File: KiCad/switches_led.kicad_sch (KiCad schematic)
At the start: 70 parts, among them Q2 MMBT3904, Q3 MMBT3904, Q4 MMBT3904, Q5 MMBT3904, Q6 MMBT3904, Q7 MMBT3904, Q8 MMBT3904, Q9 MMBT3904, SW8 SW_Rotary_1x9_MP, U2 CD4017BE

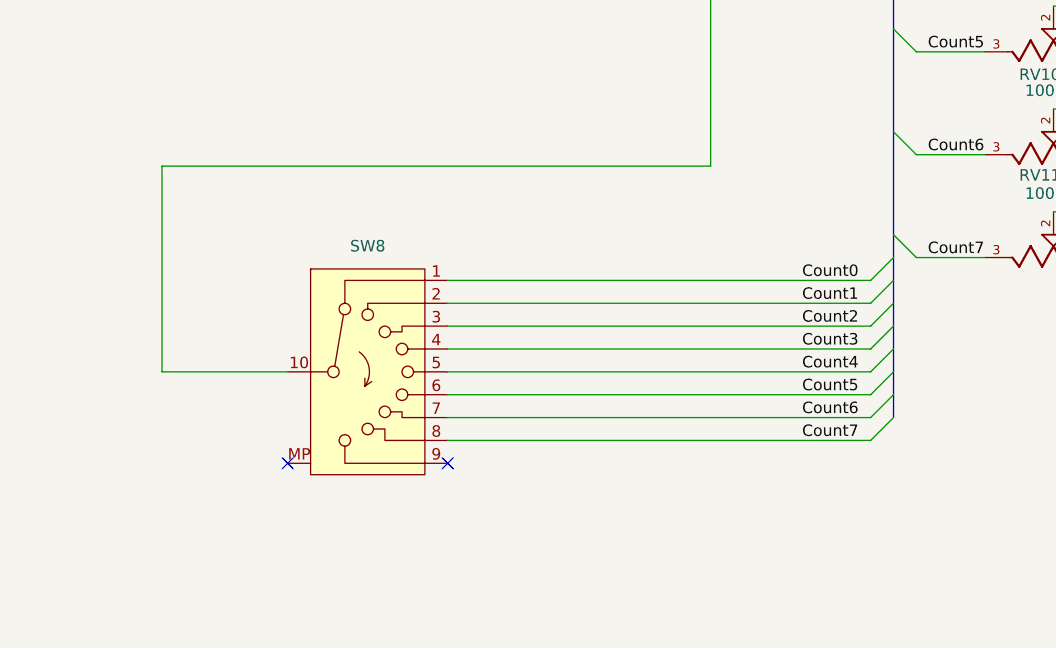
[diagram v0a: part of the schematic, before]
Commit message: adding footprint for rotary switch P1S8
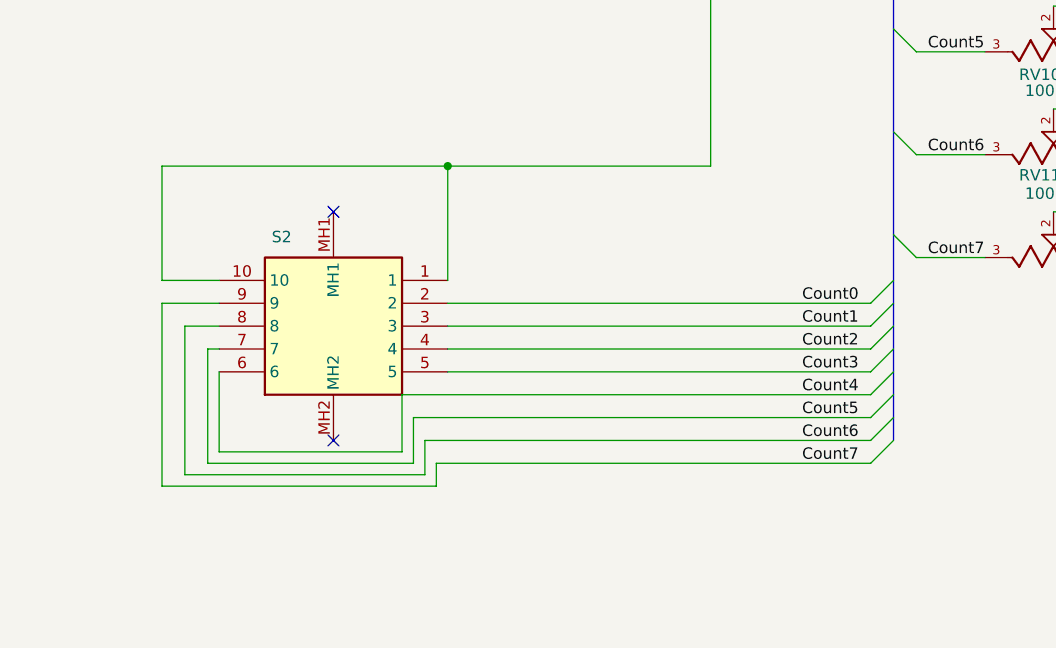
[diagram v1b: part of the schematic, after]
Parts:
- removed SW8: SW_Rotary_1x9_MP, symbol Switch:SW_Rotary_1x9_MP
- added S2: SR1712F-0108-20F0A-N9-N-027, Eurorack:1 Pole 8 Step Switch Alpha, symbol Eurorack:SR1712F-0108-20F0A-N9-N-027
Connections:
- net Count0: now also S2.2
- net Count1: now also S2.3
- net Count2: now also S2.4
- net Count3: now also S2.5
- net Count4: now also S2.6
- net Count5: now also S2.7
- net Count6: now also S2.8
- net Count7: now also S2.9
- net EXTERNAL RESET: now also S2.1, S2.10

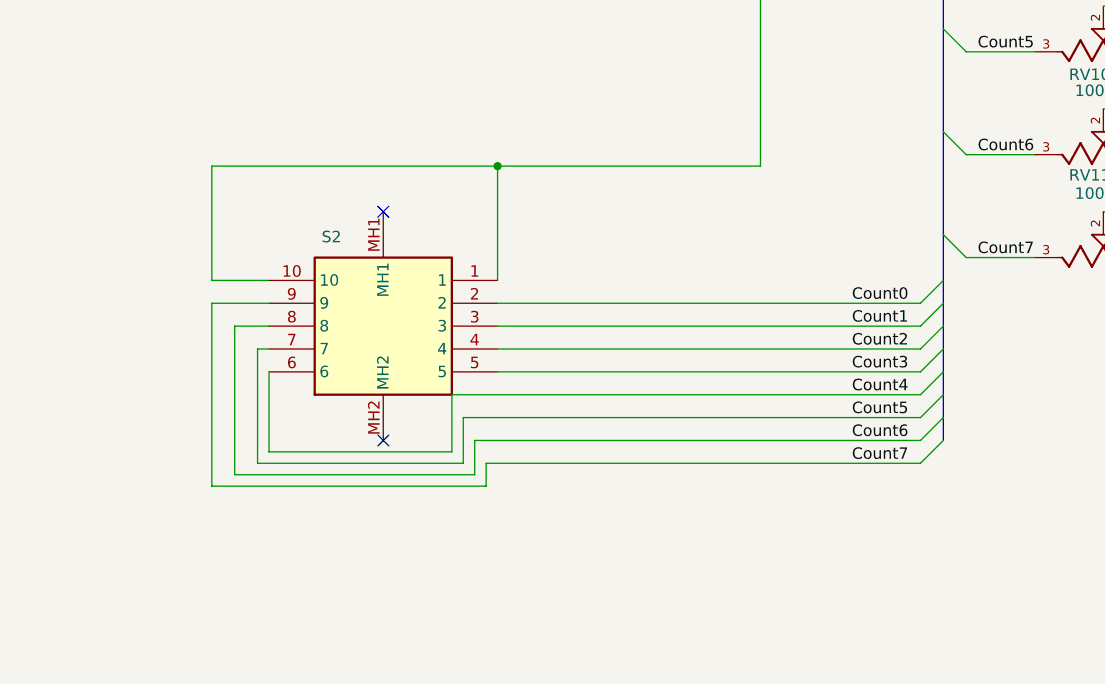
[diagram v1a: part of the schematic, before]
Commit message: adding new rotary switch
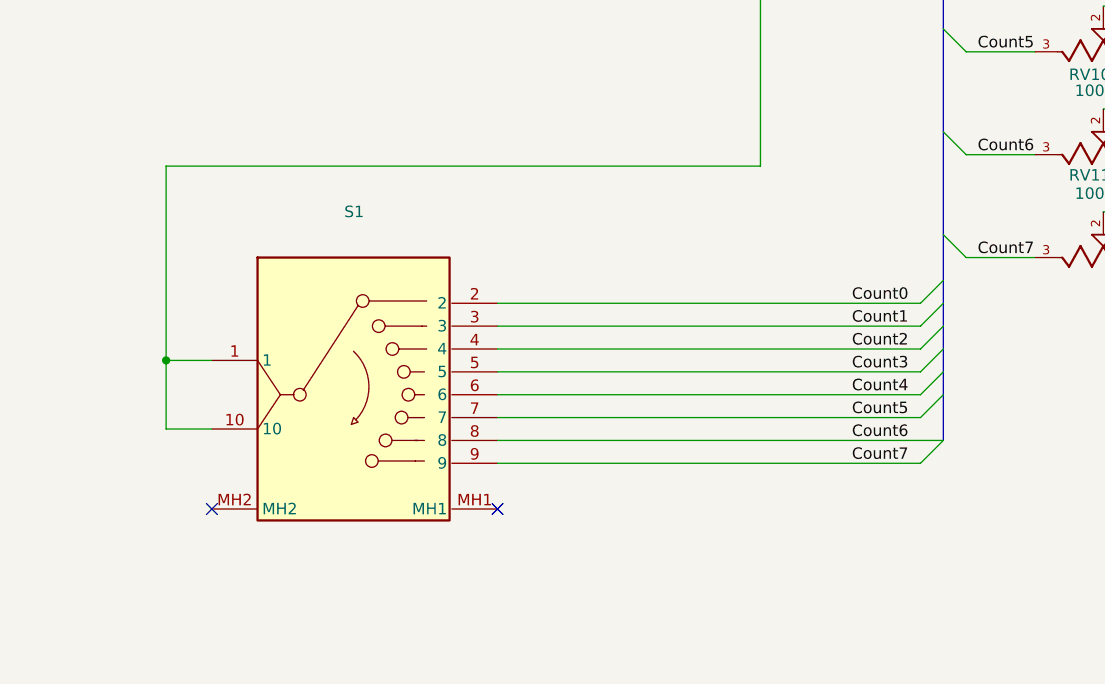
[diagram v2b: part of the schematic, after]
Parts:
- removed S2: SR1712F-0108-20F0A-N9-N-027, Eurorack:1 Pole 8 Step Switch Alpha, symbol Eurorack:SR1712F-0108-20F0A-N9-N-027
- added S1: SR1712F-0108-20F0A-N9-N-027, Eurorack:1 Pole 8 Step Switch Alpha, symbol Eurorack:SR1712F-0108-20F0A-N9-N-027
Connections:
- net Count0: now also S1.2
- net Count1: now also S1.3
- net Count2: now also S1.4
- net Count3: now also S1.5
- net Count4: now also S1.6
- net Count5: now also S1.7
- net Count6: now also S1.8
- net Count7: now also S1.9
- net EXTERNAL RESET: now also S1.1, S1.10

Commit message: placing layout frontview
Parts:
- RV10, RV11, RV4, RV5, RV6, RV7, RV8, RV9: footprint Eurorack:RD901F -> Eurorack:RD901F_1
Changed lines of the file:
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@@
 	(title_block
 		(title "8 Step Sequencer")
-		(date "2026-03-13")
+		(date "2026-03-21")
 		(rev "v1.0")
 		(company "Dirty Dream - Nathanael Noir")
@@
 			)
 		)
-		(property "Footprint" "Eurorack:RD901F"
+		(property "Footprint" "Eurorack:RD901F_1"
 			(at 247.65 52.07 0)
 			(effects
@@
 			)
 		)
-		(property "Footprint" "Eurorack:RD901F"
+		(property "Footprint" "Eurorack:RD901F_1"
 			(at 247.65 64.77 0)
 			(effects
@@
 			)
 		)
-		(property "Footprint" "Eurorack:RD901F"
+		(property "Footprint" "Eurorack:RD901F_1"
 			(at 247.65 111.76 0)
 			(effects
@@
 			)
 		)
-		(property "Footprint" "Eurorack:RD901F"
+		(property "Footprint" "Eurorack:RD901F_1"
 			(at 247.65 76.2 0)
 			(effects
@@
 			)
 		)
-		(property "Footprint" "Eurorack:RD901F"
+		(property "Footprint" "Eurorack:RD901F_1"
 			(at 247.65 100.33 0)
 			(effects
@@
 			)
 		)
-		(property "Footprint" "Eurorack:RD901F"
+		(property "Footprint" "Eurorack:RD901F_1"
 			(at 247.65 123.19 0)
 			(effects
@@
 			)
 		)
-		(property "Footprint" "Eurorack:RD901F"
+		(property "Footprint" "Eurorack:RD901F_1"
 			(at 247.65 88.9 0)
 			(effects
@@
 			)
 		)
-		(property "Footprint" "Eurorack:RD901F"
+		(property "Footprint" "Eurorack:RD901F_1"
 			(at 247.65 39.37 0)
 			(effects

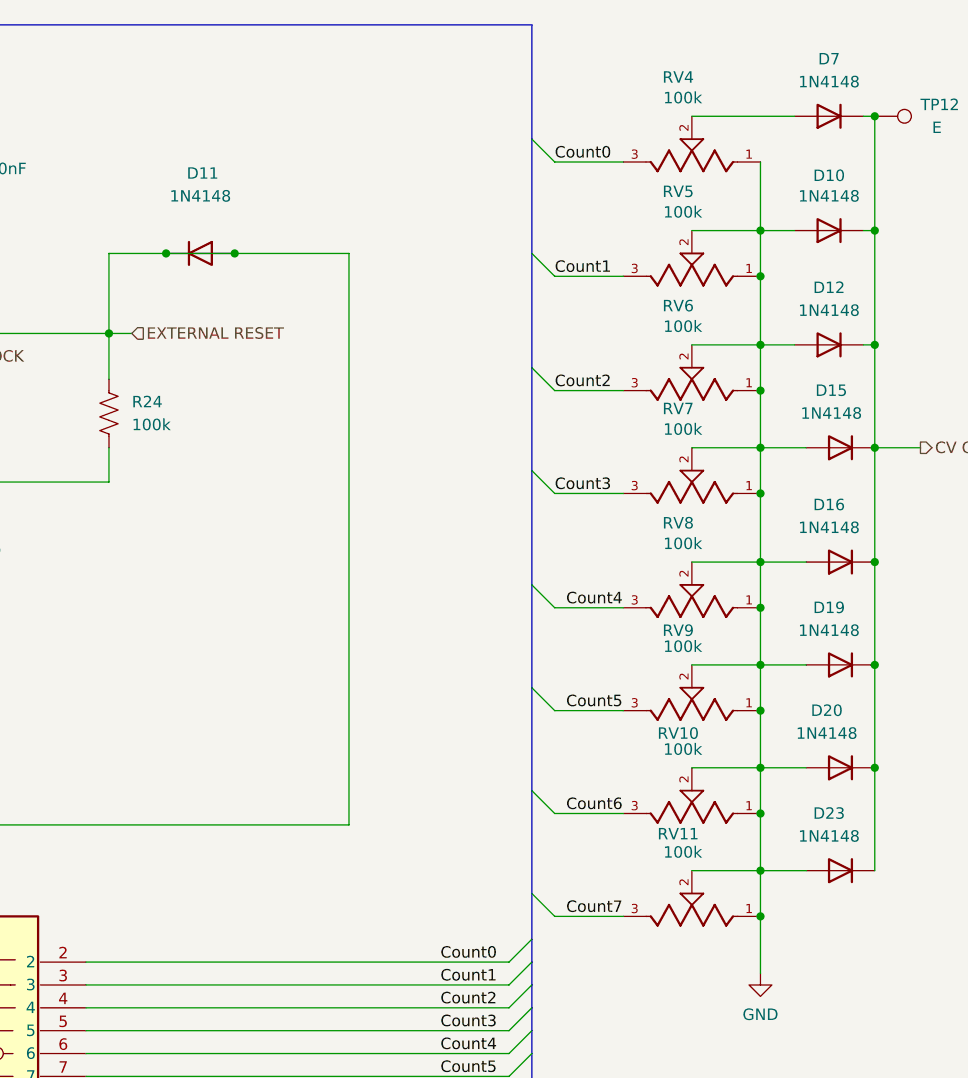
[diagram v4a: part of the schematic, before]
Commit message: fixing some errors in schematics; first component placement
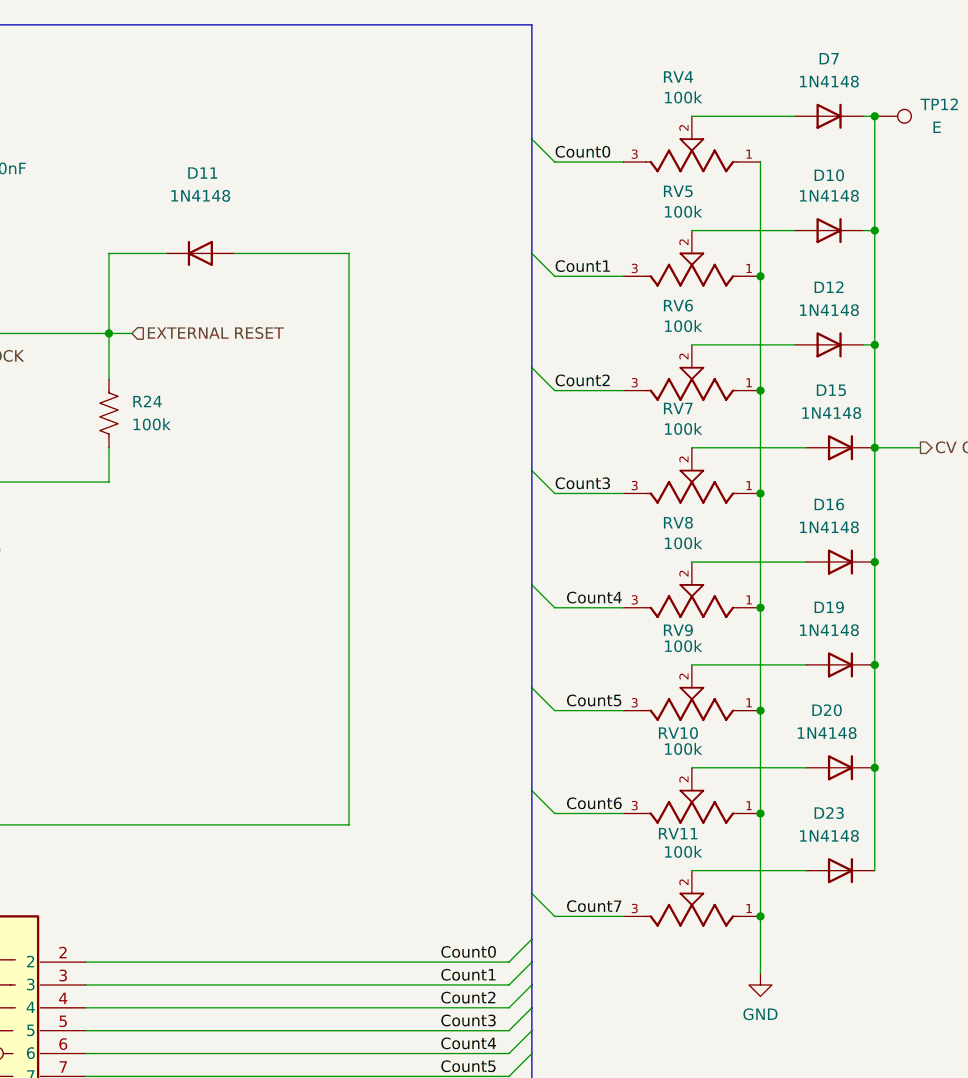
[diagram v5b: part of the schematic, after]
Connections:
- net EXTERNAL RESET: no longer D11.2 (A), S1.1, S1.10
- net GND: no longer D10.2 (A), D12.2 (A), D15.2 (A), D16.2 (A), D19.2 (A), D20.2 (A), D23.2 (A), RV10.2, RV11.2, RV5.2, RV6.2, RV7.2, RV8.2, RV9.2
- new net: D11.2 (A), S1.1, S1.10
- new net: D23.2 (A), RV11.2
- new net: D10.2 (A), RV5.2
- new net: D16.2 (A), RV8.2
- new net: D12.2 (A), RV6.2
- new net: D20.2 (A), RV10.2
- new net: D15.2 (A), RV7.2
- new net: D19.2 (A), RV9.2
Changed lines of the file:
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@@
-	)
-	(junction
-		(at 189.23 49.53)
-		(diameter 0)
-		(color 0 0 0 0)
 	)
 	(junction
@@
 	)
 	(junction
-		(at 255.27 83.82)
-		(diameter 0)
-		(color 0 0 0 0)
-	)
-	(junction
 		(at 19.05 90.17)
 		(diameter 0)
@@
 	)
 	(junction
-		(at 255.27 59.69)
-		(diameter 0)
-		(color 0 0 0 0)
-	)
-	(junction
 		(at 59.69 29.21)
 		(diameter 0)
@@
 	)
 	(junction
-		(at 255.27 46.99)
-		(diameter 0)
-		(color 0 0 0 0)
-	)
-	(junction
 		(at 83.82 90.17)
 		(diameter 0)
@@
 	)
 	(junction
-		(at 255.27 95.25)
-		(diameter 0)
-		(color 0 0 0 0)
-	)
-	(junction
 		(at 267.97 34.29)
 		(diameter 0)
@@
 	)
 	(junction
-		(at 196.85 49.53)
-		(diameter 0)
-		(color 0 0 0 0)
-	)
-	(junction
 		(at 19.05 160.02)
 		(diameter 0)
@@
 	)
 	(junction
-		(at 255.27 106.68)
-		(diameter 0)
-		(color 0 0 0 0)
-	)
-	(junction
-		(at 255.27 118.11)
-		(diameter 0)
-		(color 0 0 0 0)
-	)
-	(junction
 		(at 255.27 76.2)
-		(diameter 0)
-		(color 0 0 0 0)
-	)
-	(junction
-		(at 255.27 71.12)
 		(diameter 0)
 		(color 0 0 0 0)
@@
 		)
 	)
-	(wire
-		(pts
-			(xy 196.85 49.53) (xy 189.23 49.53)
-		)
-		(stroke
-			(width 0)
-			(type default)
-		)
-	)
-	(wire
-		(pts
-			(xy 255.27 52.07) (xy 255.27 59.69)
-		)
-		(stroke
-			(width 0)
-			(type default)
-		)
-	)
 	(bus
 		(pts
@@
 	(wire
 		(pts
-			(xy 255.27 95.25) (xy 260.35 95.25)
+			(xy 247.65 95.25) (xy 260.35 95.25)
 		)
 		(stroke
@@
 	(wire
 		(pts
-			(xy 255.27 106.68) (xy 260.35 106.68)
-		)
-		(stroke
-			(width 0)
-			(type default)
-		)
-	)
-	(wire
-		(pts
-			(xy 255.27 88.9) (xy 255.27 95.25)
-		)
-		(stroke
-			(width 0)
-			(type default)
-		)
-	)
-	(wire
-		(pts
 			(xy 83.82 90.17) (xy 83.82 113.03)
 		)
@@
 	(wire
 		(pts
-			(xy 255.27 59.69) (xy 255.27 64.77)
+			(xy 255.27 52.07) (xy 255.27 64.77)
 		)
 		(stroke
@@
 	(wire
 		(pts
-			(xy 255.27 59.69) (xy 259.08 59.69)
+			(xy 247.65 59.69) (xy 259.08 59.69)
 		)
 		(stroke
@@
 	(wire
 		(pts
-			(xy 255.27 95.25) (xy 255.27 100.33)
+			(xy 255.27 88.9) (xy 255.27 100.33)
 		)
 		(stroke
@@
 	(wire
 		(pts
-			(xy 247.65 46.99) (xy 255.27 46.99)
-		)
-		(stroke
-			(width 0)
-			(type default)
-		)
-	)
-	(wire
-		(pts
-			(xy 247.65 106.68) (xy 255.27 106.68)
+			(xy 247.65 46.99) (xy 259.08 46.99)
+		)
+		(stroke
+			(width 0)
+			(type default)
+		)
+	)
+	(wire
+		(pts
+			(xy 247.65 106.68) (xy 260.35 106.68)
 		)
 		(stroke
@@
 	(wire
 		(pts
-			(xy 255.27 71.12) (xy 255.27 76.2)
-		)
-		(stroke
-			(width 0)
-			(type default)
-		)
-	)
-	(wire
-		(pts
-			(xy 255.27 118.11) (xy 255.27 123.19)
+			(xy 255.27 111.76) (xy 255.27 123.19)
 		)
 		(stroke
@@
 	(wire
 		(pts
-			(xy 255.27 39.37) (xy 255.27 46.99)
-		)
-		(stroke
-			(width 0)
-			(type default)
-		)
-	)
-	(wire
-		(pts
 			(xy 180.34 143.51) (xy 229.87 143.51)
 		)
@@
 	(wire
 		(pts
-			(xy 247.65 95.25) (xy 255.27 95.25)
-		)
-		(stroke
-			(width 0)
-			(type default)
-		)
-	)
-	(wire
-		(pts
 			(xy 36.83 113.03) (xy 33.02 113.03)
 		)
@@
 	(wire
 		(pts
-			(xy 255.27 46.99) (xy 255.27 52.07)
+			(xy 255.27 39.37) (xy 255.27 52.07)
 		)
 		(stroke
@@
 		)
 	)
-	(wire
-		(pts
-			(xy 247.65 83.82) (xy 255.27 83.82)
-		)
-		(stroke
-			(width 0)
-			(type default)
-		)
-	)
 	(bus
 		(pts
@@
 	(wire
 		(pts
-			(xy 255.27 100.33) (xy 255.27 106.68)
+			(xy 255.27 100.33) (xy 255.27 111.76)
 		)
 		(stroke
@@
 	(wire
 		(pts
-			(xy 255.27 83.82) (xy 255.27 88.9)
-		)
-		(stroke
-			(width 0)
-			(type default)
-		)
-	)
-	(wire
-		(pts
 			(xy 36.83 45.72) (xy 33.02 45.72)
 		)
@@
 	(wire
 		(pts
-			(xy 255.27 71.12) (xy 260.35 71.12)
+			(xy 247.65 71.12) (xy 260.35 71.12)
 		)
 		(stroke
@@
 	(wire
 		(pts
-			(xy 255.27 83.82) (xy 260.35 83.82)
+			(xy 247.65 83.82) (xy 260.35 83.82)
 		)
 		(stroke
@@
 		)
 	)
-	(wire
-		(pts
-			(xy 255.27 46.99) (xy 259.08 46.99)
-		)
-		(stroke
-			(width 0)
-			(type default)
-		)
-	)
 	(bus
 		(pts
@@
 	(wire
 		(pts
-			(xy 255.27 118.11) (xy 260.35 118.11)
-		)
-		(stroke
-			(width 0)
-			(type default)
-		)
-	)
-	(wire
-		(pts
 			(xy 267.97 95.25) (xy 267.97 106.68)
 		)
@@
 	(wire
 		(pts
-			(xy 247.65 71.12) (xy 255.27 71.12)
-		)
-		(stroke
-			(width 0)
-			(type default)
-		)
-	)
-	(wire
-		(pts
 			(xy 19.05 45.72) (xy 19.05 67.31)
 		)
@@
 	(wire
 		(pts
-			(xy 255.27 111.76) (xy 255.27 118.11)
-		)
-		(stroke
-			(width 0)
-			(type default)
-		)
-	)
-	(wire
-		(pts
 			(xy 158.75 86.36) (xy 158.75 71.12)
 		)
@@
 	(wire
 		(pts
-			(xy 255.27 106.68) (xy 255.27 111.76)
-		)
-		(stroke
-			(width 0)
-			(type default)
-		)
-	)
-	(wire
-		(pts
 			(xy 59.69 72.39) (xy 59.69 78.74)
 		)
@@
 	(wire
 		(pts
-			(xy 255.27 64.77) (xy 255.27 71.12)
-		)
-		(stroke
-			(width 0)
-			(type default)
-		)
-	)
-	(wire
-		(pts
-			(xy 255.27 76.2) (xy 255.27 83.82)
+			(xy 255.27 64.77) (xy 255.27 76.2)
+		)
+		(stroke
+			(width 0)
+			(type default)
+		)
+	)
+	(wire
+		(pts
+			(xy 255.27 76.2) (xy 255.27 88.9)
 		)
 		(stroke
@@
 	(wire
 		(pts
-			(xy 247.65 118.11) (xy 255.27 118.11)
+			(xy 247.65 118.11) (xy 260.35 118.11)
 		)
 		(stroke
@@
 		)
 		(stroke
-			(width 0)
-			(type default)
-		)
-	)
-	(wire
-		(pts
-			(xy 247.65 59.69) (xy 255.27 59.69)
-		)
-		(stroke
